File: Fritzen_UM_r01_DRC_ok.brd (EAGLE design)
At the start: 68.6 x 53.3 mm, 28 parts, among them IC1 7805T, Q1 16MHz, X1 POWERSUPPLY_DC21MMX, X2 Ser_Comm

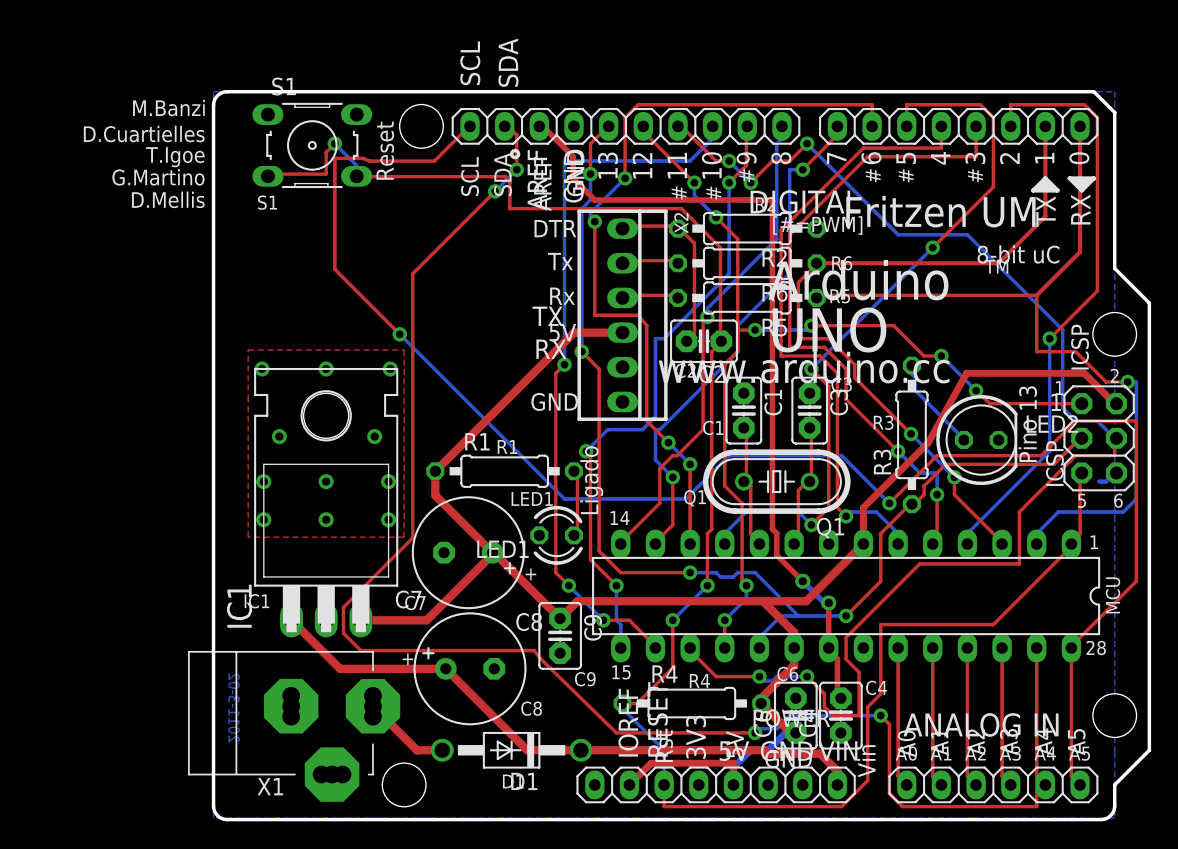
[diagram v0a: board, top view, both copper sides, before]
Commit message: Second release of the PCB and schematic
Corrections made to the PCB  silkcreen and traces (due to clearances and
other issues). Please do not produce any version older than this one.
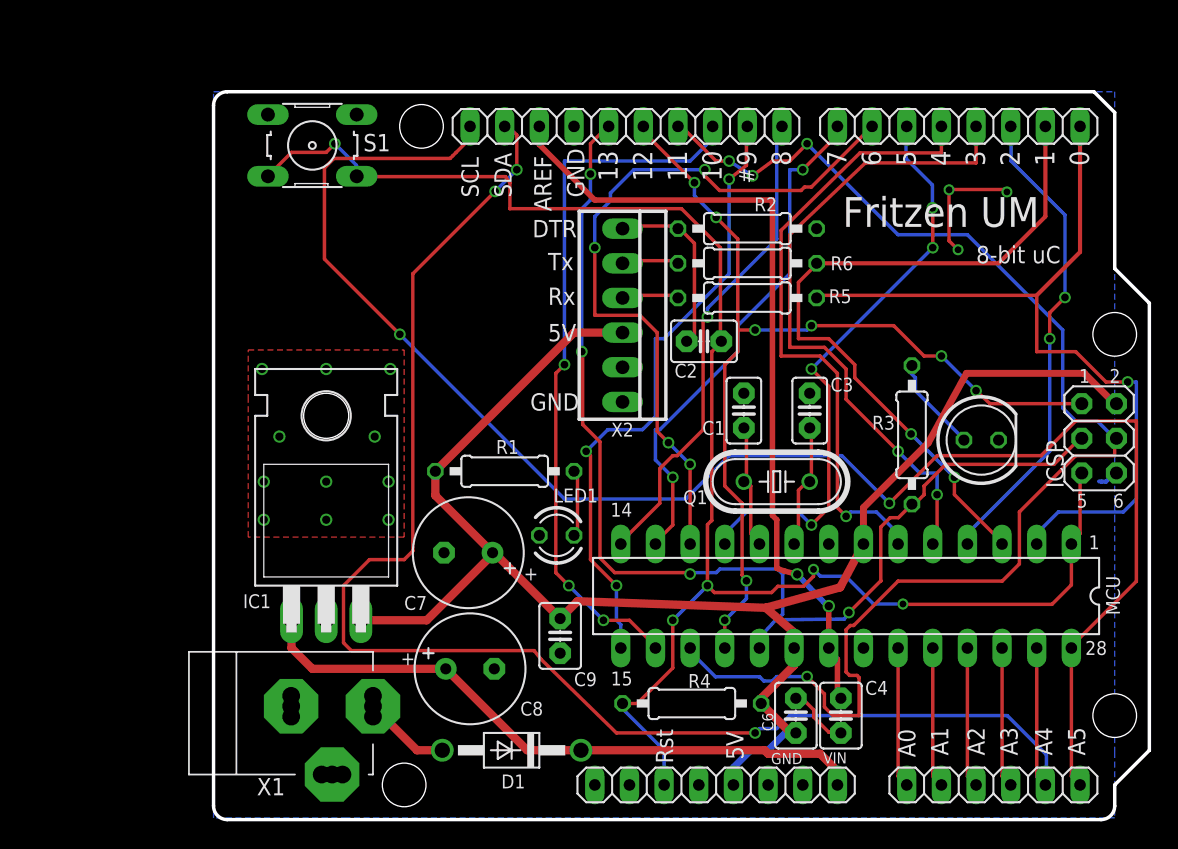
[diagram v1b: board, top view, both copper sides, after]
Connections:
- net +5V: no longer POWER.2
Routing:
- net RESET: track 135.4 -> 121.5 mm, vias 3 -> 5
- net GND: track 1.53 -> 15.2 mm, vias 11 -> 14
- net IO5: track 52.9 -> 42.9 mm, vias 3 -> 4
- net +5V: track 125.6 -> 115.6 mm
- net IO2: track 43.5 -> 35.2 mm, vias 1 -> 2
- net IO6: track 57.2 -> 53.7 mm
- net AD4/SDA: track 115.5 -> 113.6 mm, vias 4 -> 3
- net SCK: track 82.2 -> 84.1 mm
- net VIN: track 45.6 -> 46.8 mm
- net AD5/SCL: track 119.0 -> 120.1 mm
- net MOSI: track 97.6 -> 97.7 mm, vias 5 -> 4
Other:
- board text removed: "2011-3-02"
- board text removed: "3V3"
- board text removed: "ANALOG IN"
- board text removed: "ATMEGA328"
- board text removed: "Arduino"
- board text removed: "D.Cuartielles"
- board text removed: "D.Mellis"
- board text removed: "DIGITAL"
- board text removed: "G.Martino"
- board text removed: "ICSP"
- board text removed: "IOREF"
- board text removed: "ITALY"
- board text removed: "L"
- board text removed: "Ligado"
- board text removed: "M.Banzi"
- board text removed: "MADE IN"
- board text removed: "ON"
- board text removed: "PC1"
- board text removed: "PC2"
- board text removed: "Pino 13"
- board text removed: "RESET"
- board text removed: "RX"
- board text removed: "Reset"
- board text removed: "S1"
- board text removed: "T.Igoe"
- board text removed: "TM"
- board text removed: "TX"
- board text removed: "UNO"
- board text removed: "Vin"
- board text removed: "[#=PWM]"
- board text removed: "designed by"
- board text removed: "tinker it"
- board text removed: "www.arduino.cc"

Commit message: Cleaning PCB and Fabrication files
I have order 30 pieces of this board revision at MakerStudio.cc
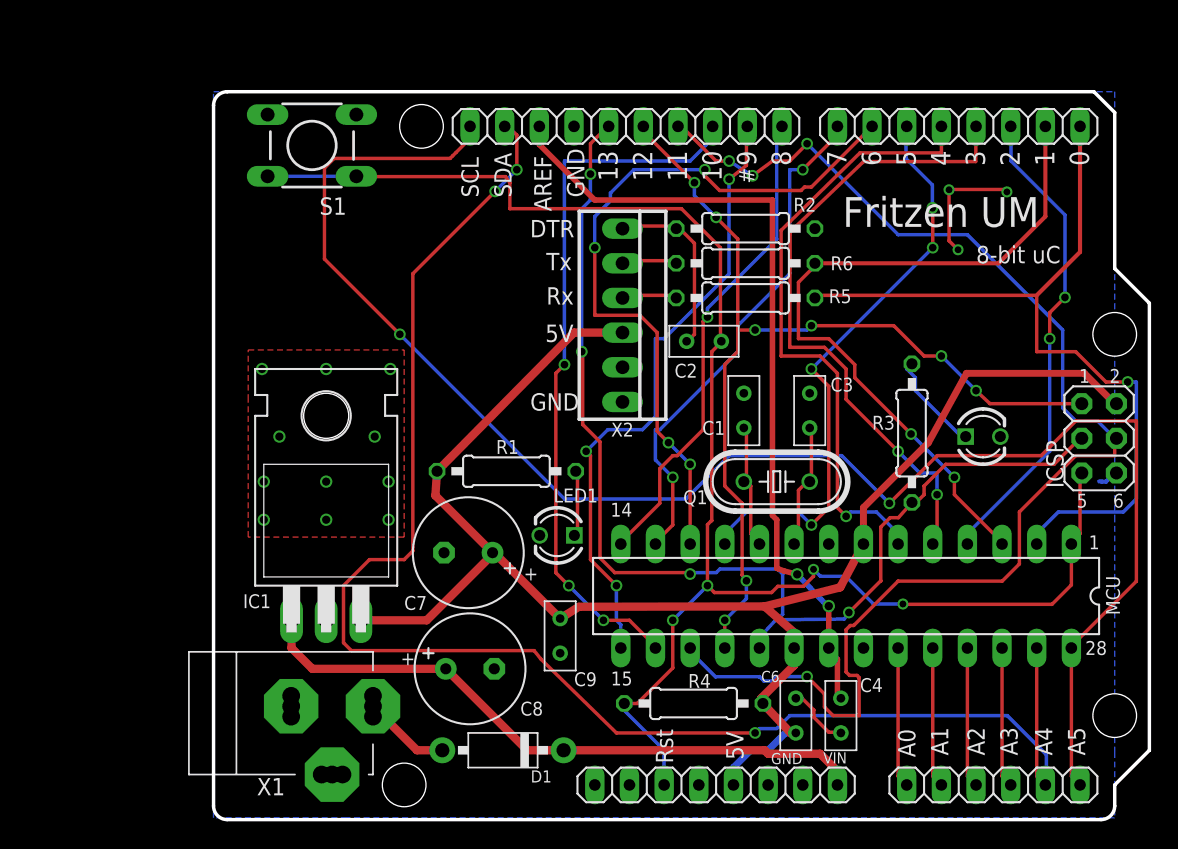
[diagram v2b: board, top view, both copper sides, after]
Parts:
- removed LED1: PWR_LED, led:LED3MM
- removed LED2: PIN13, led:LED5MM
- added D2: CX-G302DC, Seeed-OPL-Diode:LED2-2.54-D3.0MM
- added D3: SR302DC, Seeed-OPL-Diode:LED2-2.54-D3.0MM
- C1, C3: value 22pF -> 22pf; device capacitor-wima:C2.5-2 -> Seeed-OPL-Capacitor:CERAMIC-2.54
- C2, C4, C6, C9: value 100nF -> 100nf; device capacitor-wima:C2.5-3 -> Seeed-OPL-Capacitor:CERAMIC-2.54
- D1: device diode:DO41-10 -> Seeed-OPL-Diode:DO-41
- Q1: value 16MHz -> 16MHZ; device crystal:HC49/S -> Seeed-OPL-Crystal-Oscillator:HC49US
- R1, R2, R3, R4, R5, R6: value 1k -> 1K; device rcl:0207/10 -> Seeed-OPL-Resistor:PR-D2.3XL6.5MM
- S1: value Reset -> TACTILE-SWITCH-PTH; device switch-omron:B3F-10XX -> GeekAmmo:TAC-SWITCH-PTH
- moved D1 0.64 mm to (21.2, 5.08), turned to 0 degrees
- turned S1 to 180 degrees
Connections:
- net GND: now also D2.K, D3.K, S1.3, S1.4; no longer LED1.K, LED2.K, S1.1, S1.2
- net N$2: now also D2.A; no longer LED2.A
- net N$3: now also D3.A; no longer LED1.A
- net PWRIN: now also D1.1; no longer D1.A
- net RESET: now also S1.1, S1.2; no longer S1.3, S1.4
- net VIN: now also D1.2; no longer D1.C
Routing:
- net RESET: track 121.5 -> 119.0 mm, vias 5 -> 4
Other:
- board text removed: "D1"
